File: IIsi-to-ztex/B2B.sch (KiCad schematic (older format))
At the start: 8 parts, among them J1 Conn_02x07_Odd_Even

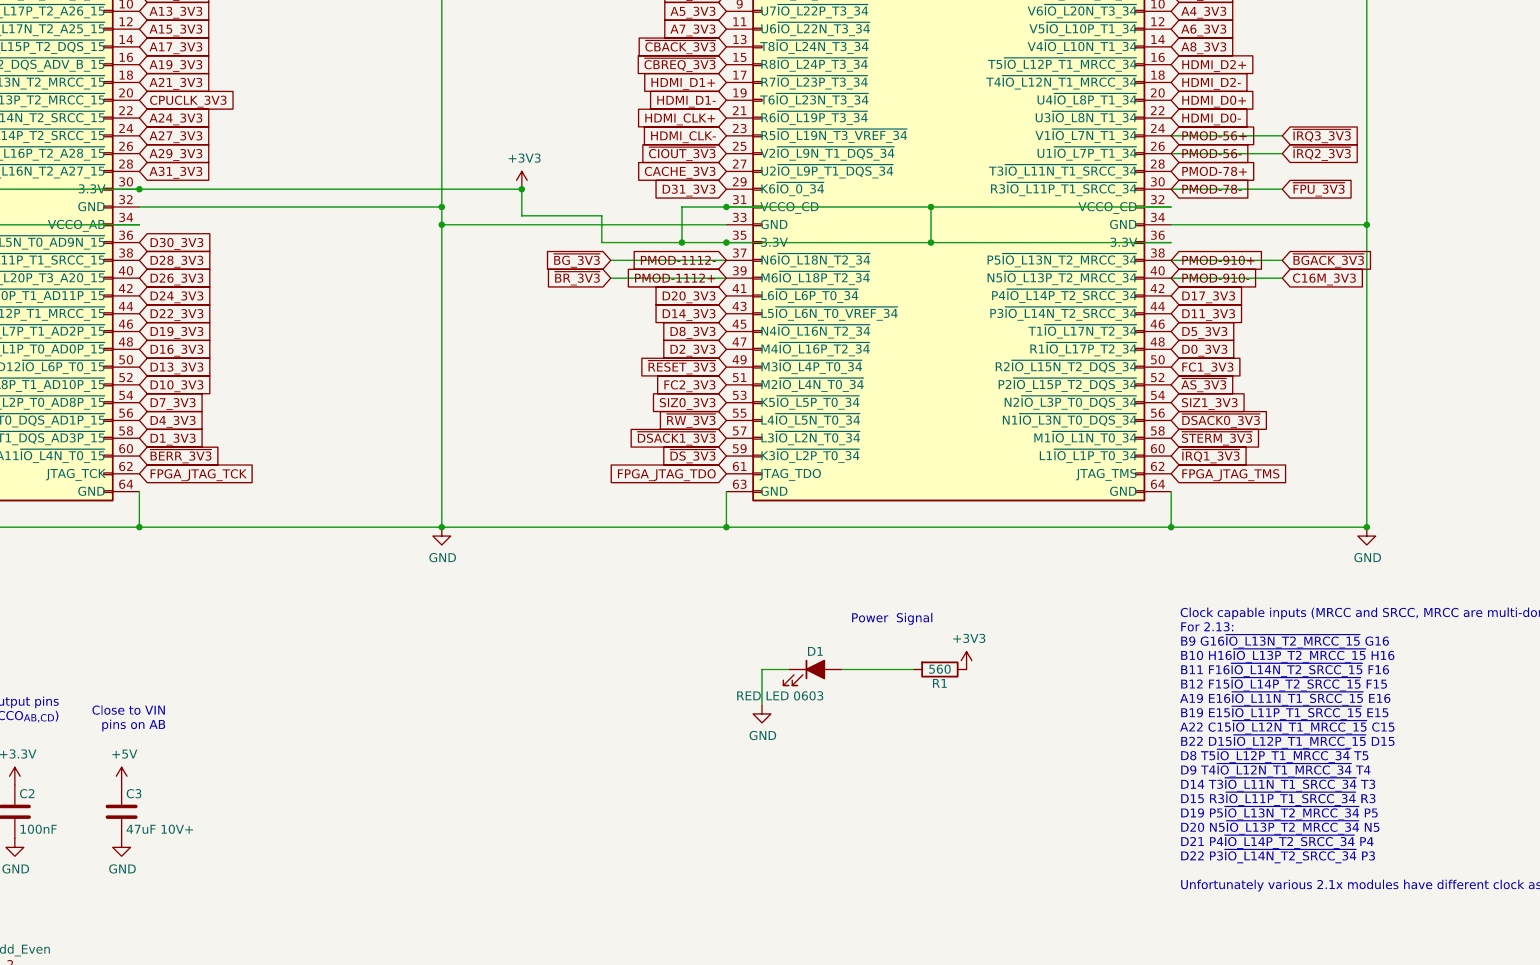
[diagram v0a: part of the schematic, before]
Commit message: 3V3 SRAM draft
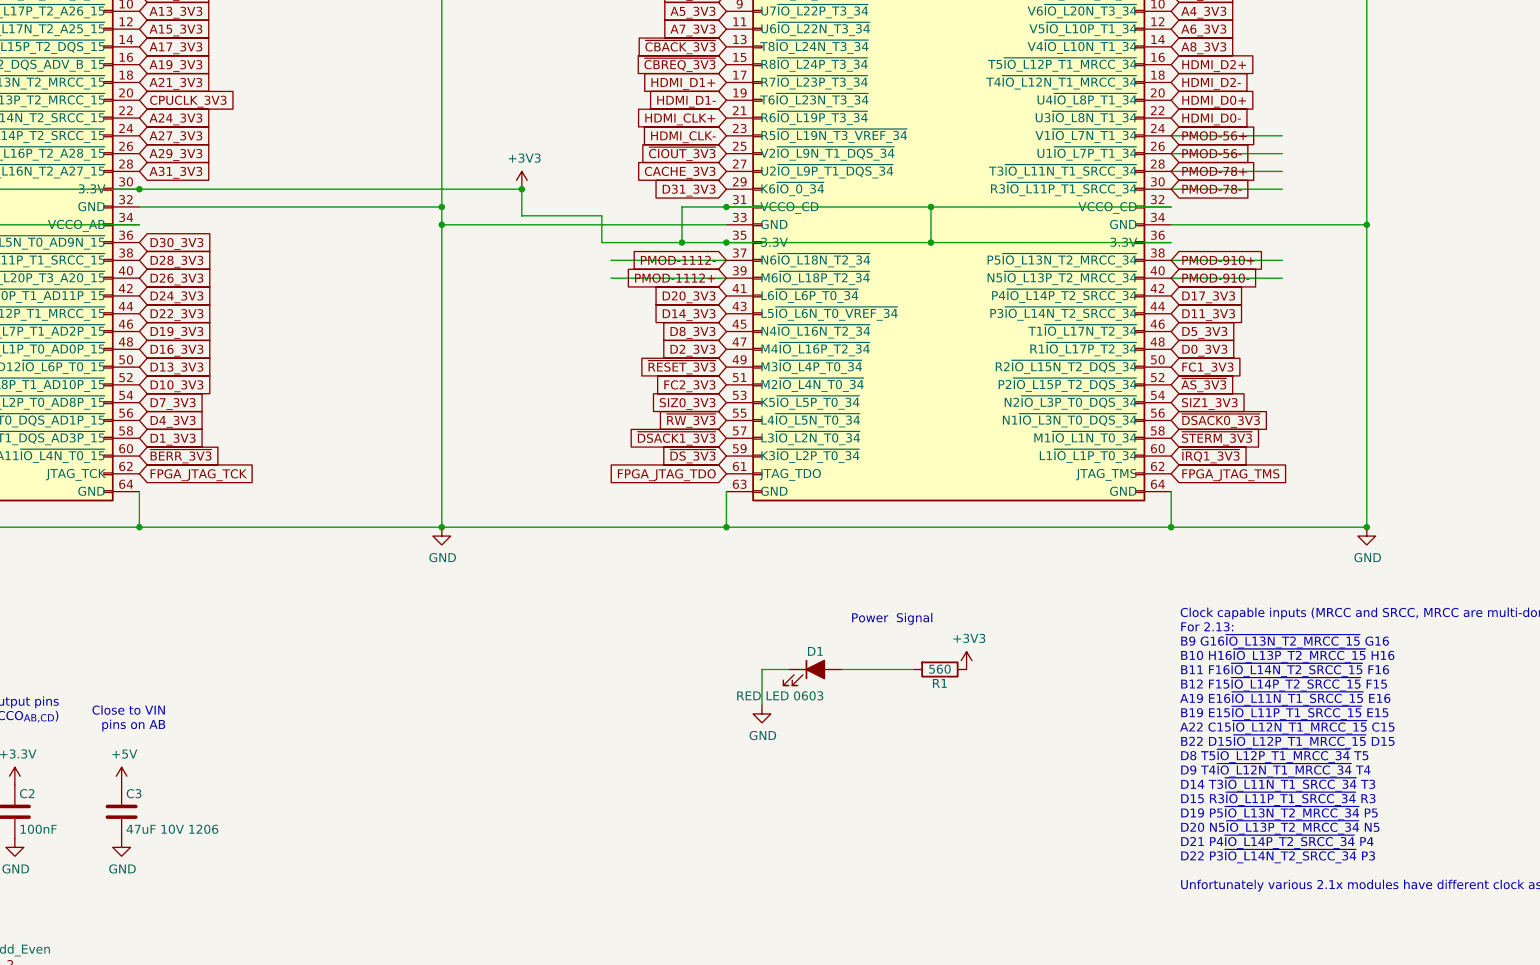
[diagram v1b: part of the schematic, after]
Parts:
- C1, C2: footprint Capacitor_SMD:C_0603_1608Metric -> Capacitor_SMD:C_0402_1005Metric; LCSC ? -> (none); MNF1_URL www.yageo.com -> (none); MPN CC0603KRX7R9BB104 -> CL05B104KO5NNNC; Mouser 603-CC603KRX7R8BB104 -> (none); URL https://www.lcsc.com/product-detail/Multilayer-Ceramic-Capa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 -> (none)
- C3: value 47uF 10V+ -> 47uF 10V 1206
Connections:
- net labels removed: C16M_3V3, ~BGACK_3V3, ~BG_3V3, ~BR_3V3, ~FPU_3V3, ~IRQ2_3V3, ~IRQ3_3V3
- wire segments 67 -> 68
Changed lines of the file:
@@
 $Descr A4 11693 8268
 encoding utf-8
-Sheet 2 5
+Sheet 2 6
 Title "nubus-to-ztex B2B connector"
 Date ""
@@
 F 0 "C1" H 3025 6150 50  0000 L CNN
 F 1 "100nF" H 3025 5950 50  0000 L CNN
-F 2 "Capacitor_SMD:C_0603_1608Metric" H 3038 5900 50  0001 C CNN
+F 2 "Capacitor_SMD:C_0402_1005Metric" H 3038 5900 50  0001 C CNN
 F 3 "" H 3000 6050 50  0000 C CNN
-F 4 "www.yageo.com" H 3000 6050 50  0001 C CNN "MNF1_URL"
-F 5 "CC0603KRX7R9BB104" H 3000 6050 50  0001 C CNN "MPN"
-F 6 "603-CC603KRX7R8BB104" H 3000 6050 50  0001 C CNN "Mouser"
+F 4 "" H 3000 6050 50  0001 C CNN "MNF1_URL"
+F 5 "CL05B104KO5NNNC" H 3000 6050 50  0001 C CNN "MPN"
+F 6 "" H 3000 6050 50  0001 C CNN "Mouser"
 F 7 "?" H 3000 6050 50  0001 C CNN "Digikey"
-F 8 "?" H 3000 6050 50  0001 C CNN "LCSC"
+F 8 "" H 3000 6050 50  0001 C CNN "LCSC"
 F 9 "?" H 3000 6050 50  0001 C CNN "Koncar"
 F 10 "TB" H 3000 6050 50  0001 C CNN "Side"
-F 11 "https://www.lcsc.com/product-detail/Multilayer-Ceramic-Capacitors-MLCC-SMD-SMT_YAGEO-CC0603KRX7R9BB104_C14663.html" H 3000 6050 50  0001 C CNN "URL"
+F 11 "" H 3000 6050 50  0001 C CNN "URL"
 	1    3000 6050
 	1    0    0    -1
@@
 F 0 "C2" H 3425 6150 50  0000 L CNN
 F 1 "100nF" H 3425 5950 50  0000 L CNN
-F 2 "Capacitor_SMD:C_0603_1608Metric" H 3438 5900 50  0001 C CNN
+F 2 "Capacitor_SMD:C_0402_1005Metric" H 3438 5900 50  0001 C CNN
 F 3 "" H 3400 6050 50  0000 C CNN
-F 4 "www.yageo.com" H 3400 6050 50  0001 C CNN "MNF1_URL"
-F 5 "CC0603KRX7R9BB104" H 3400 6050 50  0001 C CNN "MPN"
-F 6 "603-CC603KRX7R8BB104" H 3400 6050 50  0001 C CNN "Mouser"
+F 4 "" H 3400 6050 50  0001 C CNN "MNF1_URL"
+F 5 "CL05B104KO5NNNC" H 3400 6050 50  0001 C CNN "MPN"
+F 6 "" H 3400 6050 50  0001 C CNN "Mouser"
 F 7 "?" H 3400 6050 50  0001 C CNN "Digikey"
-F 8 "?" H 3400 6050 50  0001 C CNN "LCSC"
+F 8 "" H 3400 6050 50  0001 C CNN "LCSC"
 F 9 "?" H 3400 6050 50  0001 C CNN "Koncar"
 F 10 "TB" H 3400 6050 50  0001 C CNN "Side"
-F 11 "https://www.lcsc.com/product-detail/Multilayer-Ceramic-Capacitors-MLCC-SMD-SMT_YAGEO-CC0603KRX7R9BB104_C14663.html" H 3400 6050 50  0001 C CNN "URL"
+F 11 "" H 3400 6050 50  0001 C CNN "URL"
 	1    3400 6050
 	1    0    0    -1
@@
 AR Path="/6432B233/621FCA7B" Ref="C3"  Part="1"
 F 0 "C3" H 4025 6150 50  0000 L CNN
-F 1 "47uF 10V+" H 4025 5950 50  0000 L CNN
+F 1 "47uF 10V 1206" H 4025 5950 50  0000 L CNN
 F 2 "Capacitor_SMD:C_1206_3216Metric" H 4038 5900 50  0001 C CNN
 F 3 "" H 4000 6050 50  0000 C CNN
@@
 Text GLabel 7400 2350 0    50   Input ~ 0
 ~CIOUT_3V3
-Text GLabel 10525 2950 2    50   Input ~ 0
-~BGACK_3V3
-Text GLabel 6750 2950 0    50   Input ~ 0
-~BG_3V3
-Text GLabel 6750 3050 0    50   Input ~ 0
-~BR_3V3
-Text GLabel 10525 2550 2    50   Input ~ 0
-~FPU_3V3
 Wire Wire Line
 	10525 2950 9900 2950
@@
 Wire Wire Line
 	6750 2950 7400 2950
-Text GLabel 10525 3050 2    50   Input ~ 0
-C16M_3V3
 Wire Wire Line
 	9900 2550 10525 2550
-Text GLabel 10525 2250 2    50   Input ~ 0
-~IRQ3_3V3
-Text GLabel 10525 2350 2    50   Input ~ 0
-~IRQ2_3V3
 Wire Wire Line
 	9900 2350 10525 2350
 Wire Wire Line
 	10525 2250 9900 2250
+Wire Wire Line
+	10525 2450 9900 2450
 $EndSCHEMATC
